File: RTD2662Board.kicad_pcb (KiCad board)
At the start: 2 copper layers, 100 x 70 mm, 263 parts, among them J1 DVI, J10 UART/I2C, J11 LCD Connector, J12 SPDIFF, J13 3.5mm jack, J14 DC Jack, J15 Expansion Connector, J2 HDMI A, J3 3.5mm jack, J4 VGA, J5 CVBS1, J6 CVBS2, J7 Mini-DIN-4, J8 USB B, J9 Keyboard Connector, Q1 BC846, Q2 BC846, Q3 AO3401A, Q4 BC846, Q5 AO3401A, SW1 POWER, SW2 MENU, SW3 UP, SW4 DOWN, SW5 SOURCE, U1 RTD2662, U10 25x128, U11 APW7313, U12 AMS1117-1.8, U2 TPS61040DBV, U3 TL1838, U4 CH341T, U5 TPS61040DBV, U6 ES7134S, U7 PAM8003, U8 TPS61040DBV, U9 24x01, Y1 27MHz, Y2 12MHz

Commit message: Finalising
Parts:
- removed R11, R12, R7, R8: 330Ω, Resistor_SMD:R_0402_1005Metric_Pad0.72x0.64mm_HandSolder
- C11, C13, C3, C5: value 33pF -> 270pF
- C12, C14, C4, C6: value 82pF -> 820pF
- L1, L2, L3, L4: value 8.2uH -> 1uH
- R64: value 15kΩ -> 1.5kΩ
- R71: value 6.8kΩ -> 680Ω
- RV1: value 10kΩ -> 1kΩ
- U7: footprint RTD2662Board:HSOP-16-1EP_3.9x9.9mm_P1.27mm_EP2.41x4.1mm -> Package_SO:SO-16_3.9x9.9mm_P1.27mm
- moved C75 54.6 mm to (160.8, 110.5)
- moved C1 54.6 mm to (189.8, 80.2)
- moved C10 54.6 mm to (188.0, 92.5)
- moved C11 54.6 mm to (182.8, 76.0)
- moved C12 54.6 mm to (184.8, 78.2)
- moved C13 54.6 mm to (186.0, 88.8)
- moved C14 54.6 mm to (188.0, 91.0)
- moved C15 54.6 mm to (184.0, 80.2)
- moved C16 54.6 mm to (186.0, 91.8)
- moved C17 54.6 mm to (178.2, 109.2)
- moved C18 54.6 mm to (178.2, 110.5)
- moved C19 54.6 mm to (191.2, 120.0)
- moved C2 54.6 mm to (186.8, 95.0)
- moved C20 54.6 mm to (182.8, 111.0)
- moved C21 54.6 mm to (187.0, 119.2)
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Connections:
- C72 pad 1: +1V8 -> +3V3
- C74 pad 1: +1V8 -> +3V3
- FB1 pad 1: Net-(FB1-Pad1) -> Net-(C3-Pad1)
- FB2 pad 1: Net-(FB2-Pad1) -> Net-(C5-Pad1)
- FB3 pad 1: Net-(FB3-Pad1) -> Net-(C11-Pad1)
- FB4 pad 1: Net-(FB4-Pad1) -> Net-(C13-Pad1)
- J1 pad 12: Net-(J1-Pad12) -> unconnected-(J1-Pad12)
- J1 pad 13: Net-(J1-Pad13) -> unconnected-(J1-Pad13)
- J1 pad 20: Net-(J1-Pad20) -> unconnected-(J1-Pad20)
- J1 pad 21: Net-(J1-Pad21) -> unconnected-(J1-Pad21)
- J1 pad 4: Net-(J1-Pad4) -> unconnected-(J1-Pad4)
- J1 pad 5: Net-(J1-Pad5) -> unconnected-(J1-Pad5)
- J1 pad 8: Net-(J1-Pad8) -> unconnected-(J1-Pad8)
- J1 pad C1: Net-(J1-PadC1) -> unconnected-(J1-PadC1)
- J1 pad C2: Net-(J1-PadC2) -> unconnected-(J1-PadC2)
- J1 pad C3: Net-(J1-PadC3) -> unconnected-(J1-PadC3)
- J1 pad C4: Net-(J1-PadC4) -> unconnected-(J1-PadC4)
- J11 pad 10: Net-(J11-Pad10) -> unconnected-(J11-Pad10)
- J11 pad 8: Net-(J11-Pad8) -> unconnected-(J11-Pad8)
- J11 pad 9: Net-(J11-Pad9) -> unconnected-(J11-Pad9)
- J4 pad 11: Net-(J4-Pad11) -> unconnected-(J4-Pad11)
- J4 pad 4: Net-(J4-Pad4) -> unconnected-(J4-Pad4)
- J4 pad 9: Net-(J4-Pad9) -> unconnected-(J4-Pad9)
- R10 pad 1: Net-(FB2-Pad1) -> Net-(C5-Pad1)
- R13 pad 1: Net-(FB3-Pad1) -> Net-(C11-Pad1)
- R14 pad 1: Net-(FB4-Pad1) -> Net-(C13-Pad1)
- R9 pad 1: Net-(FB1-Pad1) -> Net-(C3-Pad1)
- U1 pad 28: Net-(U1-Pad28) -> unconnected-(U1-Pad28)
- U1 pad 39: Net-(U1-Pad39) -> unconnected-(U1-Pad39)
- U4 pad 14: Net-(U4-Pad14) -> unconnected-(U4-Pad14)
- U4 pad 17: Net-(U4-Pad17) -> unconnected-(U4-Pad17)
- U4 pad 18: Net-(U4-Pad18) -> unconnected-(U4-Pad18)
- U4 pad 2: Net-(U4-Pad2) -> unconnected-(U4-Pad2)
- U4 pad 5: Net-(U4-Pad5) -> unconnected-(U4-Pad5)
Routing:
- net +1V8: track 158.5 -> 136.9 mm, vias 6 -> 5
- net +3V3: track 462.8 -> 472.0 mm, vias 25 -> 27
- net Net-(C13-Pad1): track 2.83 -> 7.53 mm
- net GND: track 248.4 -> 244.7 mm, vias 319 -> 311
- net Net-(C5-Pad1): track 2.78 -> 6.50 mm
- net Net-(C3-Pad1): track 2.83 -> 6.31 mm
- net Net-(C11-Pad1): track 2.97 -> 6.45 mm
- net Net-(FB3-Pad1): track 2.93 -> 0.00 mm
- net Net-(FB1-Pad1): track 2.93 -> 0.00 mm
- net Net-(FB4-Pad1): track 2.90 -> 0.00 mm
- net Net-(FB2-Pad1): track 2.90 -> 0.00 mm
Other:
- board text added: "ORTD2662-PROTOBOARD-REV2"
- board text removed: "ORTD2662-PROTOBOARD-REV1"

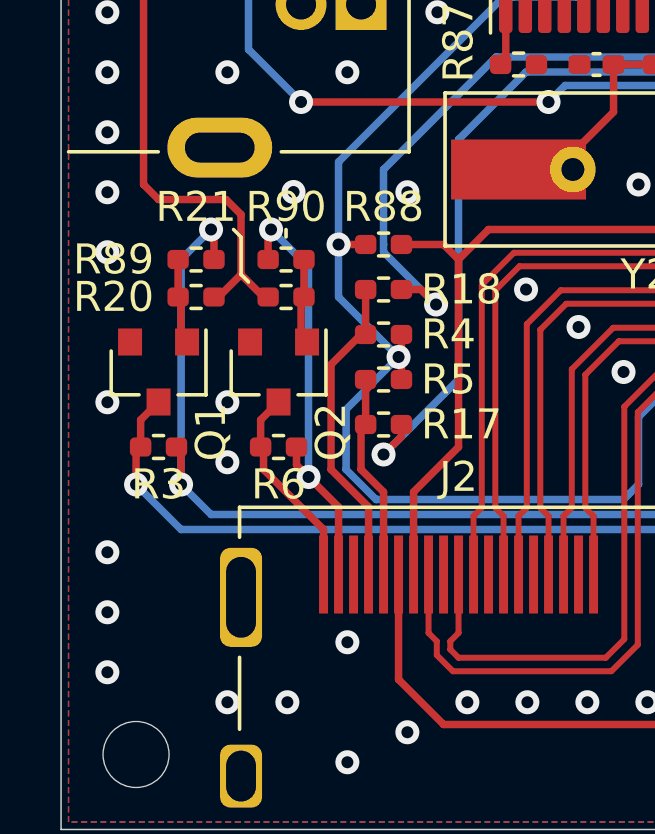
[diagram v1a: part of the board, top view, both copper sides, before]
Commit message: Added an extra 3.3v filtering cap, fixed label positions in schematic
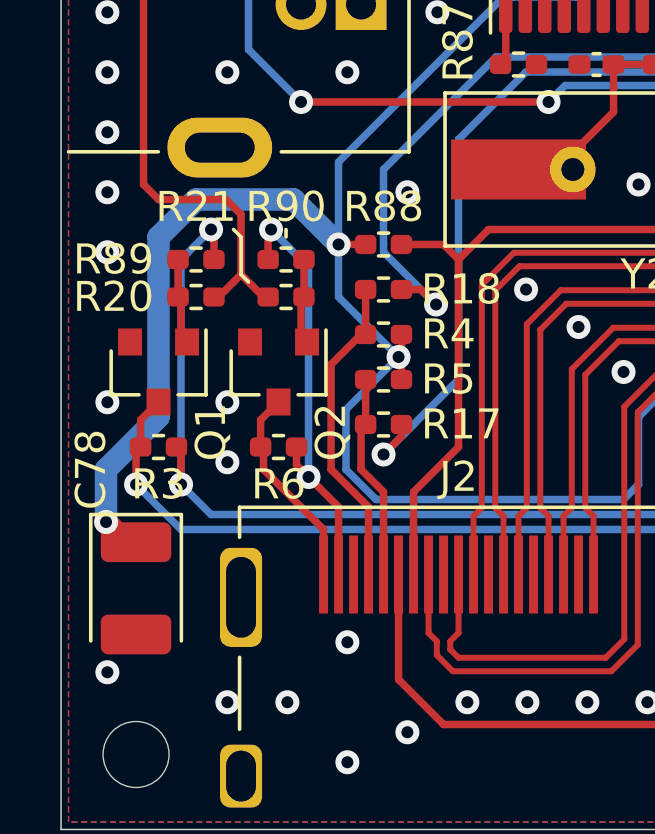
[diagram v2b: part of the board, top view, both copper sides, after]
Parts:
- added C78: 100uF, Capacitor_Tantalum_SMD:CP_EIA-3528-21_Kemet-B, F.Cu at (102.5, 122.0)
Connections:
- C50 pad 1: Net-(C50-Pad1) -> Net-(U7-VREF)
- C52 pad 1: Net-(C52-Pad1) -> Net-(U7-VOL)
- R61 pad 1: Net-(R61-Pad1) -> Net-(U7-LIN)
- R63 pad 1: Net-(R63-Pad1) -> Net-(U7-RIN)
- R69 pad 1: Net-(C52-Pad1) -> Net-(U7-VOL)
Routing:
- net +3V3: track 472.0 -> 490.6 mm, vias 27 -> 28
- net GND: vias 311 -> 308
